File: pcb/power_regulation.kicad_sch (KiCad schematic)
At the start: 46 parts, among them U6 TPS563201, U7 TPS563201, U8 LM1085-5.0, U9 AMS1117-3.3

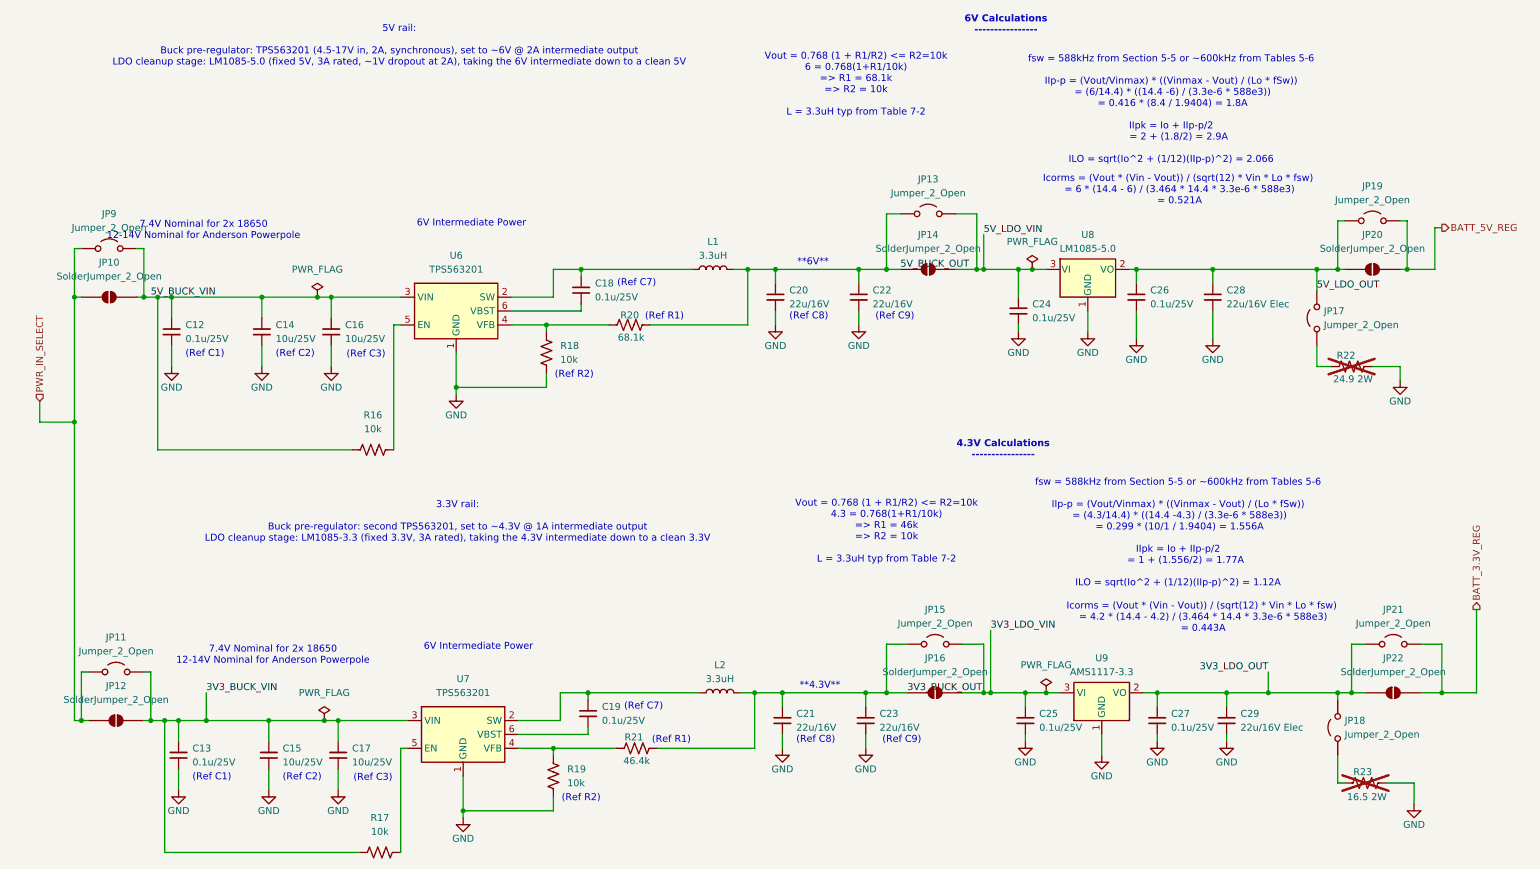
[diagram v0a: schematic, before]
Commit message: updated battery regulation circuit to bump up intermediate voltages
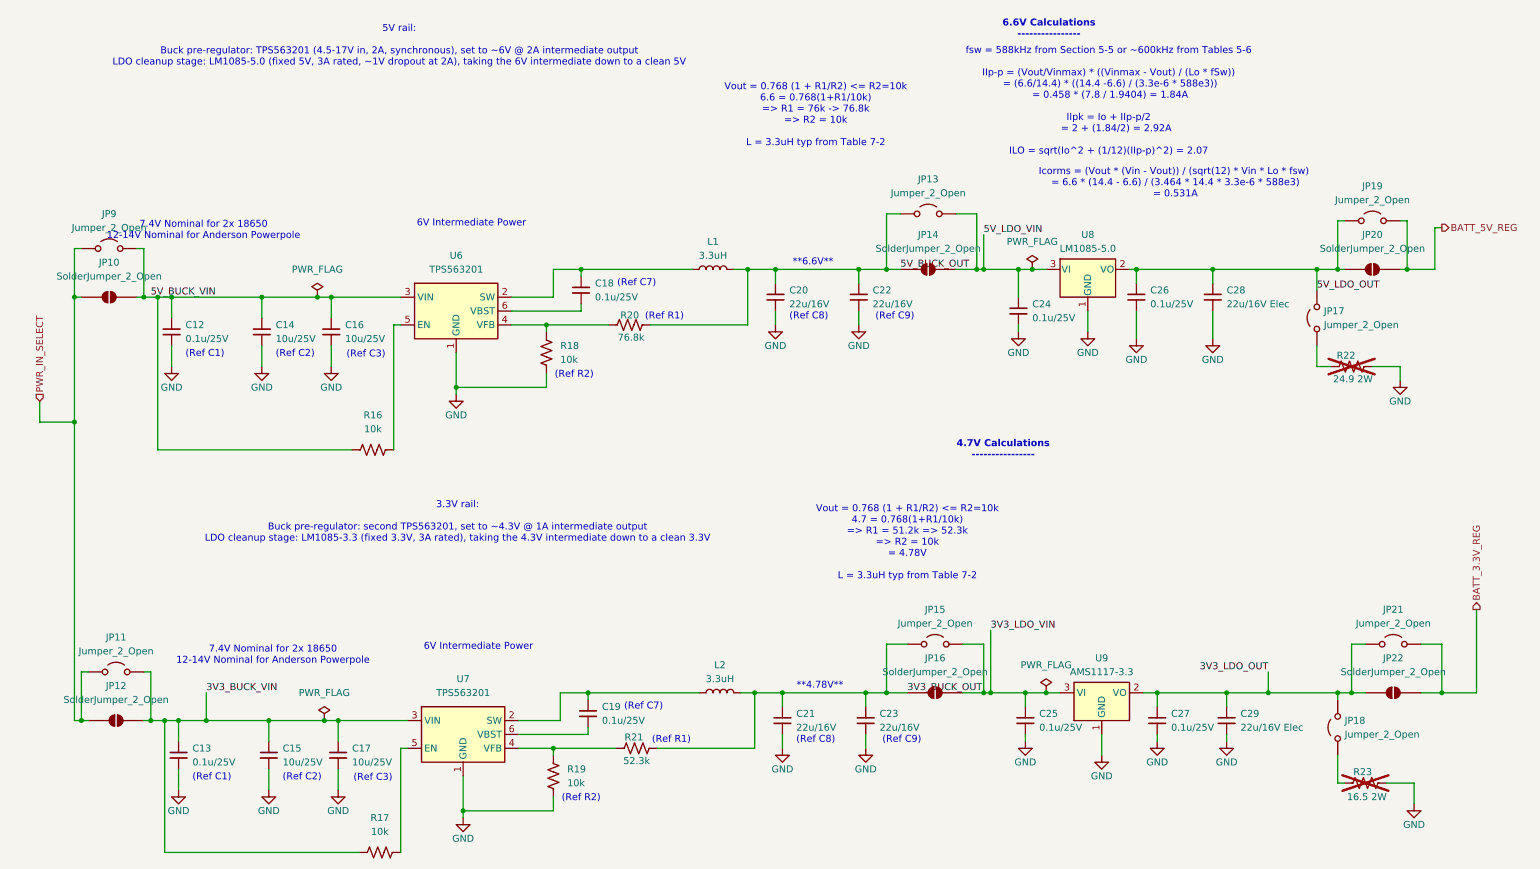
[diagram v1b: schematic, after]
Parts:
- R18, R19: footprint Resistor_SMD:R_0805_2012Metric -> Resistor_SMD:R_0603_1608Metric; LCSC Part # C84376 -> C95204; MPN RC0805FR-0710KL -> RT0603BRD0710KL; Package 0805 -> 0603
- R20: value 68.1k -> 76.8k; footprint Resistor_SMD:R_0201_0603Metric -> Resistor_SMD:R_0603_1608Metric; LCSC Part # C228015 -> C705795; MPN AC0603FR-0768K1L -> RT0603BRD0776K8L
- R21: value 46.4k -> 52.3k; footprint Resistor_SMD:R_0805_2012Metric -> Resistor_SMD:R_0603_1608Metric; LCSC Part # C483162 -> C861462; MPN RC0805FR-0746K4L -> RT0603BRD0752K3L; Package 0805 -> 0603
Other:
- note added: "**4.78V**"
- note added: "**6.6V**"
- note added: "4.7V Calculations ----------------"
- note added: "6.6V Calculations ----------------"
- note added: "Icorms = (Vout * (Vin - Vout)) / (sqrt(12) * Vin * Lo * fsw) = 6.6 * (14.4 - 6.6) / (3.464 * 14.4 * 3.3e-6 * 588e3) = 0.531A"
- note added: "Vout = 0.768 (1 + R1/R2) <= R2=10k 4.7 = 0.768(1+R1/10k) => R1 = 51.2k => 52.3k => R2 = 10k = 4.78V L = 3.3uH typ from Table 7-2"
- note added: "Vout = 0.768 (1 + R1/R2) <= R2=10k 6.6 = 0.768(1+R1/10k) => R1 = 76k -> 76.8k => R2 = 10k L = 3.3uH typ from Table 7-2"
- note added: "fsw = 588kHz from Section 5-5 or ~600kHz from Tables 5-6 IIp-p = (Vout/Vinmax) * ((Vinmax - Vout) / (Lo * fSw)) = (6.6/14.4) * ((14.4 -6.6) / (3.3e-6 * 588e3)) = 0.458 * (7.8 / 1.9404) = 1.84A IIpk = Io + IIp-p/2 = 2 + (1.84/2) = 2.92A ILO = sqrt(Io^2 + (1/12)(IIp-p)^2) = 2.07"
- note removed: "**4.3V**"
- note removed: "**6V**"
- note removed: "4.3V Calculations ----------------"
- note removed: "6V Calculations ----------------"
- note removed: "Icorms = (Vout * (Vin - Vout)) / (sqrt(12) * Vin * Lo * fsw) = 4.2 * (14.4 - 4.2) / (3.464 * 14.4 * 3.3e-6 * 588e3) = 0.443A"
- note removed: "Icorms = (Vout * (Vin - Vout)) / (sqrt(12) * Vin * Lo * fsw) = 6 * (14.4 - 6) / (3.464 * 14.4 * 3.3e-6 * 588e3) = 0.521A"
- note removed: "Vout = 0.768 (1 + R1/R2) <= R2=10k 4.3 = 0.768(1+R1/10k) => R1 = 46k => R2 = 10k L = 3.3uH typ from Table 7-2"
- note removed: "Vout = 0.768 (1 + R1/R2) <= R2=10k 6 = 0.768(1+R1/10k) => R1 = 68.1k => R2 = 10k L = 3.3uH typ from Table 7-2"
- note removed: "fsw = 588kHz from Section 5-5 or ~600kHz from Tables 5-6 IIp-p = (Vout/Vinmax) * ((Vinmax - Vout) / (Lo * fSw)) = (4.3/14.4) * ((14.4 -4.3) / (3.3e-6 * 588e3)) = 0.299 * (10/1 / 1.9404) = 1.556A IIpk = Io + IIp-p/2 = 1 + (1.556/2) = 1.77A ILO = sqrt(Io^2 + (1/12)(IIp-p)^2) = 1.12A"
- note removed: "fsw = 588kHz from Section 5-5 or ~600kHz from Tables 5-6 IIp-p = (Vout/Vinmax) * ((Vinmax - Vout) / (Lo * fSw)) = (6/14.4) * ((14.4 -6) / (3.3e-6 * 588e3)) = 0.416 * (8.4 / 1.9404) = 1.8A IIpk = Io + IIp-p/2 = 2 + (1.8/2) = 2.9A ILO = sqrt(Io^2 + (1/12)(IIp-p)^2) = 2.066"
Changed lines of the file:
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@@
 		)
 	)
-	(text "Icorms = (Vout * (Vin - Vout)) / (sqrt(12) * Vin * Lo * fsw)\n = 4.2 * (14.4 - 4.2) / (3.464 * 14.4 * 3.3e-6 * 588e3)\n = 0.443A"
+	(text "6V Intermediate Power"
 		(exclude_from_sim no)
-		(at 226.568 124.714 0)
+		(at 94.234 130.048 0)
 		(effects
 			(font
@@
 		)
 	)
-	(text "6V Intermediate Power"
+	(text "(Ref R2)"
 		(exclude_from_sim no)
-		(at 94.234 130.048 0)
+		(at 111.76 80.264 0)
 		(effects
 			(font
@@
 		)
 	)
-	(text "(Ref R2)"
+	(text "Vout = 0.768 (1 + R1/R2) <= R2=10k\n4.7 = 0.768(1+R1/10k) \n=> R1 = 51.2k => 52.3k\n=> R2 = 10k\n= 4.78V\n\nL = 3.3uH typ from Table 7-2"
 		(exclude_from_sim no)
-		(at 111.76 80.264 0)
+		(at 172.72 110.998 0)
 		(effects
 			(font
 				(size 1.27 1.27)
+				(thickness 0.1588)
 			)
 		)
 	)
-	(text "Vout = 0.768 (1 + R1/R2) <= R2=10k\n4.3 = 0.768(1+R1/10k) \n=> R1 = 46k\n=> R2 = 10k\n\nL = 3.3uH typ from Table 7-2"
+	(text "6.6V Calculations\n----------------"
 		(exclude_from_sim no)
-		(at 168.91 108.966 0)
+		(at 198.628 17.018 0)
 		(effects
 			(font
 				(size 1.27 1.27)
-				(thickness 0.1588)
+				(thickness 0.254)
+				(bold yes)
 			)
 		)
@@
 		)
 	)
-	(text "Vout = 0.768 (1 + R1/R2) <= R2=10k\n6 = 0.768(1+R1/10k) \n=> R1 = 68.1k\n=> R2 = 10k\n\nL = 3.3uH typ from Table 7-2"
+	(text "(Ref C2)"
 		(exclude_from_sim no)
-		(at 163.322 27.178 0)
+		(at 61.976 153.924 0)
 		(effects
 			(font
 				(size 1.27 1.27)
-				(thickness 0.1588)
 			)
 		)
 	)
-	(text "(Ref C2)"
+	(text "(Ref R1)"
 		(exclude_from_sim no)
-		(at 61.976 153.924 0)
+		(at 129.54 147.066 0)
 		(effects
 			(font
@@
 		)
 	)
-	(text "(Ref R1)"
+	(text "(Ref C8)\n\n"
 		(exclude_from_sim no)
-		(at 129.54 147.066 0)
+		(at 154.686 70.612 0)
 		(effects
 			(font
@@
 		)
 	)
-	(text "(Ref C8)\n\n"
+	(text "Icorms = (Vout * (Vin - Vout)) / (sqrt(12) * Vin * Lo * fsw)\n = 6.6 * (14.4 - 6.6) / (3.464 * 14.4 * 3.3e-6 * 588e3)\n = 0.531A"
 		(exclude_from_sim no)
-		(at 154.686 70.612 0)
+		(at 221.488 45.212 0)
 		(effects
 			(font
@@
 		)
 	)
-	(text "**6V**"
+	(text "**6.6V**"
 		(exclude_from_sim no)
 		(at 155.448 59.69 0)
@@
 		)
 	)
-	(text "4.3V Calculations\n----------------"
+	(text "4.7V Calculations\n----------------"
 		(exclude_from_sim no)
 		(at 190.246 93.98 0)
@@
 		)
 	)
-	(text "Icorms = (Vout * (Vin - Vout)) / (sqrt(12) * Vin * Lo * fsw)\n = 6 * (14.4 - 6) / (3.464 * 14.4 * 3.3e-6 * 588e3)\n = 0.521A"
-		(exclude_from_sim no)
-		(at 222.25 46.482 0)
-		(effects
-			(font
-				(size 1.27 1.27)
-			)
-		)
-	)
 	(text "(Ref C3)"
 		(exclude_from_sim no)
@@
 		)
 	)
-	(text "fsw = 588kHz from Section 5-5 or ~600kHz from Tables 5-6\n\nIIp-p = (Vout/Vinmax) * ((Vinmax - Vout) / (Lo * fSw))\n = (4.3/14.4) * ((14.4 -4.3) / (3.3e-6 * 588e3))\n = 0.299 * (10/1 / 1.9404) = 1.556A\n\nIIpk = Io + IIp-p/2\n     = 1 + (1.556/2) = 1.77A\n\nILO = sqrt(Io^2 + (1/12)(IIp-p)^2) = 1.12A"
+	(text "(Ref C9)"
 		(exclude_from_sim no)
-		(at 222.25 109.22 0)
+		(at 170.434 69.596 0)
 		(effects
 			(font
 				(size 1.27 1.27)
-				(thickness 0.1588)
 			)
 		)
 	)
-	(text "(Ref C9)"
+	(text "(Ref C7)"
 		(exclude_from_sim no)
-		(at 170.434 69.596 0)
+		(at 124.46 140.97 0)
 		(effects
 			(font
@@
 		)
 	)
-	(text "fsw = 588kHz from Section 5-5 or ~600kHz from Tables 5-6\n\nIIp-p = (Vout/Vinmax) * ((Vinmax - Vout) / (Lo * fSw))\n = (6/14.4) * ((14.4 -6) / (3.3e-6 * 588e3))\n = 0.416 * (8.4 / 1.9404) = 1.8A\n\nIIpk = Io + IIp-p/2\n     = 2 + (1.8/2) = 2.9A\n\nILO = sqrt(Io^2 + (1/12)(IIp-p)^2) = 2.066"
+	(text "(Ref C1)"
 		(exclude_from_sim no)
-		(at 220.98 31.75 0)
+		(at 44.196 76.454 0)
 		(effects
 			(font
 				(size 1.27 1.27)
-				(thickness 0.1588)
 			)
 		)
 	)
-	(text "(Ref C7)"
+	(text "fsw = 588kHz from Section 5-5 or ~600kHz from Tables 5-6\n\nIIp-p = (Vout/Vinmax) * ((Vinmax - Vout) / (Lo * fSw))\n = (6.6/14.4) * ((14.4 -6.6) / (3.3e-6 * 588e3))\n = 0.458 * (7.8 / 1.9404) = 1.84A\n\nIIpk = Io + IIp-p/2\n     = 2 + (1.84/2) = 2.92A\n\nILO = sqrt(Io^2 + (1/12)(IIp-p)^2) = 2.07"
 		(exclude_from_sim no)
-		(at 124.46 140.97 0)
+		(at 209.55 30.226 0)
 		(effects
 			(font
 				(size 1.27 1.27)
+				(thickness 0.1588)
 			)
 		)
 	)
-	(text "(Ref C1)"
+	(text "(Ref C7)"
 		(exclude_from_sim no)
-		(at 44.196 76.454 0)
+		(at 123.19 63.5 0)
 		(effects
 			(font
@@
 		)
 	)
-	(text "(Ref C7)"
+	(text "Vout = 0.768 (1 + R1/R2) <= R2=10k\n6.6 = 0.768(1+R1/10k) \n=> R1 = 76k -> 76.8k\n=> R2 = 10k\n\nL = 3.3uH typ from Table 7-2"
 		(exclude_from_sim no)
-		(at 123.19 63.5 0)
+		(at 155.956 32.766 0)
 		(effects
 			(font
 				(size 1.27 1.27)
+				(thickness 0.1588)
 			)
 		)
@@
 		)
 	)
-	(text "**4.3V**"
+	(text "**4.78V**"
 		(exclude_from_sim no)
 		(at 156.718 137.16 0)
@@
 		)
 	)
-	(text "6V Calculations\n----------------"
-		(exclude_from_sim no)
-		(at 190.754 16.256 0)
-		(effects
-			(font
-				(size 1.27 1.27)
-				(thickness 0.254)
-				(bold yes)
-			)
-		)
-	)
 	(junction
 		(at 34.29 143.51)
@@
 			)
 		)
-		(property "Footprint" "Resistor_SMD:R_0805_2012Metric"
+		(property "Footprint" "Resistor_SMD:R_0603_1608Metric"
 			(at 106.934 153.416 90)
 			(hide yes)
@@
 			)
 		)
-		(property "Datasheet" "${KIPRJMOD}/project_library/datasheets/YAGEO/RC0805FR-0710KL.pdf"
+		(property "Datasheet" "${KIPRJMOD}/project_library/datasheets/YAGEO/RT0603BRD0710KL.pdf"
 			(at 107.95 153.67 0)
 			(hide yes)
@@
 			)
 		)
-		(property "Description" "Resistor, US symbol"
+		(property "Description" "RES 10kΩ ±0.1% 100mW 0603"
 			(at 107.95 153.67 0)
 			(hide yes)
@@
 			)
 		)
-		(property "Package" "0805"
+		(property "Package" "0603"
 			(at 107.95 153.67 90)
 			(hide yes)
@@
 			)
 		)
-		(property "LCSC Part #" "C84376"
+		(property "LCSC Part #" "C95204"
 			(at 107.95 153.67 90)
 			(hide yes)
@@
 			)
 		)
-		(property "MPN" "RC0805FR-0710KL"
+		(property "MPN" "RT0603BRD0710KL"
 			(at 107.95 153.67 90)
 			(hide yes)
@@
 			)
 		)
-		(property "Value" "68.1k"
+		(property "Value" "76.8k"
 			(at 122.174 73.406 90)
 			(show_name no)
@@
 			)
 		)
-		(property "Footprint" "Resistor_SMD:R_0201_0603Metric"
+		(property "Footprint" "Resistor_SMD:R_0603_1608Metric"
 			(at 121.666 72.136 90)
 			(hide yes)
@@
 			)
 		)
-		(property "Datasheet" "${KIPRJMOD}/project_library/datasheets/YAGEO/AC0603FR-0768K1L.pdf"
+		(property "Datasheet" "${KIPRJMOD}/project_library/datasheets/YAGEO/RT0603BRD0776K8L.pdf"
 			(at 121.92 71.12 0)
 			(hide yes)
@@
 			)
 		)
-		(property "Description" "Resistor, US symbol"
+		(property "Description" "RES 76.8kΩ ±0.1% 100mW 0603"
 			(at 121.92 71.12 0)
 			(hide yes)
@@
 			)
 		)
-		(property "MPN" "AC0603FR-0768K1L"
+		(property "MPN" "RT0603BRD0776K8L"
 			(at 121.92 71.12 0)
 			(hide yes)
@@
 			)
 		)
-		(property "LCSC Part #" "C228015"
+		(property "LCSC Part #" "C705795"
 			(at 121.92 71.12 0)
 			(hide yes)
@@
 			)
 		)
-		(property "Footprint" "Resistor_SMD:R_0805_2012Metric"
+		(property "Footprint" "Resistor_SMD:R_0603_1608Metric"
 			(at 105.664 75.946 90)
 			(hide yes)
@@
 			)
 		)
-		(property "Description" "Resistor, US symbol"
+		(property "Description" "RES 10kΩ ±0.1% 100mW 0603"
 			(at 106.68 76.2 0)
 			(hide yes)
@@
 			)
 		)
-		(property "Package" "0805"
+		(property "Package" "0603"
 			(at 106.68 76.2 90)
 			(hide yes)
@@
 			)
 		)
-		(property "LCSC Part #" "C84376"
+		(property "LCSC Part #" "C95204"
 			(at 106.68 76.2 90)
 			(hide yes)
@@
 			)
 		)
-		(property "MPN" "RC0805FR-0710KL"
+		(property "MPN" "RT0603BRD0710KL"
 			(at 106.68 76.2 90)
 			(hide yes)
@@
 			)
 		)
-		(property "Value" "46.4k"
+		(property "Value" "52.3k"
 			(at 123.19 150.876 90)
 			(show_name no)
@@
 			)
 		)
-		(property "Footprint" "Resistor_SMD:R_0805_2012Metric"
+		(property "Footprint" "Resistor_SMD:R_0603_1608Metric"
 			(at 122.936 149.606 90)
 			(hide yes)
@@
 			)
 		)
-		(property "Datasheet" "${KIPRJMOD}/project_library/datasheets/YAGEO/RC0805FR-0746K4L.pdf"
+		(property "Datasheet" "${KIPRJMOD}/project_library/datasheets/YAGEO/RC0805FR-0751K1L.pdf"
 			(at 123.19 148.59 0)
 			(hide yes)
@@
 			)
 		)
-		(property "Description" "Resistor, US symbol"
+		(property "Description" "RES 52.3kΩ ±0.1% 100mW 0603"
 			(at 123.19 148.59 0)
 			(hide yes)
@@
 			)
 		)
-		(property "MPN" "RC0805FR-0746K4L"
+		(property "MPN" "RT0603BRD0752K3L"
 			(at 123.19 148.59 0)
 			(hide yes)
@@
 			)
 		)
-		(property "Package" "0805"
+		(property "Package" "0603"
 			(at 123.19 148.59 0)
 			(hide yes)
@@
 			)
 		)
-		(property "LCSC Part #" "C483162"
+		(property "LCSC Part #" "C861462"
 			(at 123.19 148.59 0)
 			(hide yes)
